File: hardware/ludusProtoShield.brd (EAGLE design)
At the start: 59.7 x 53.3 mm, 65 parts, among them U1 ARDUINO, U2 TB6612FNG

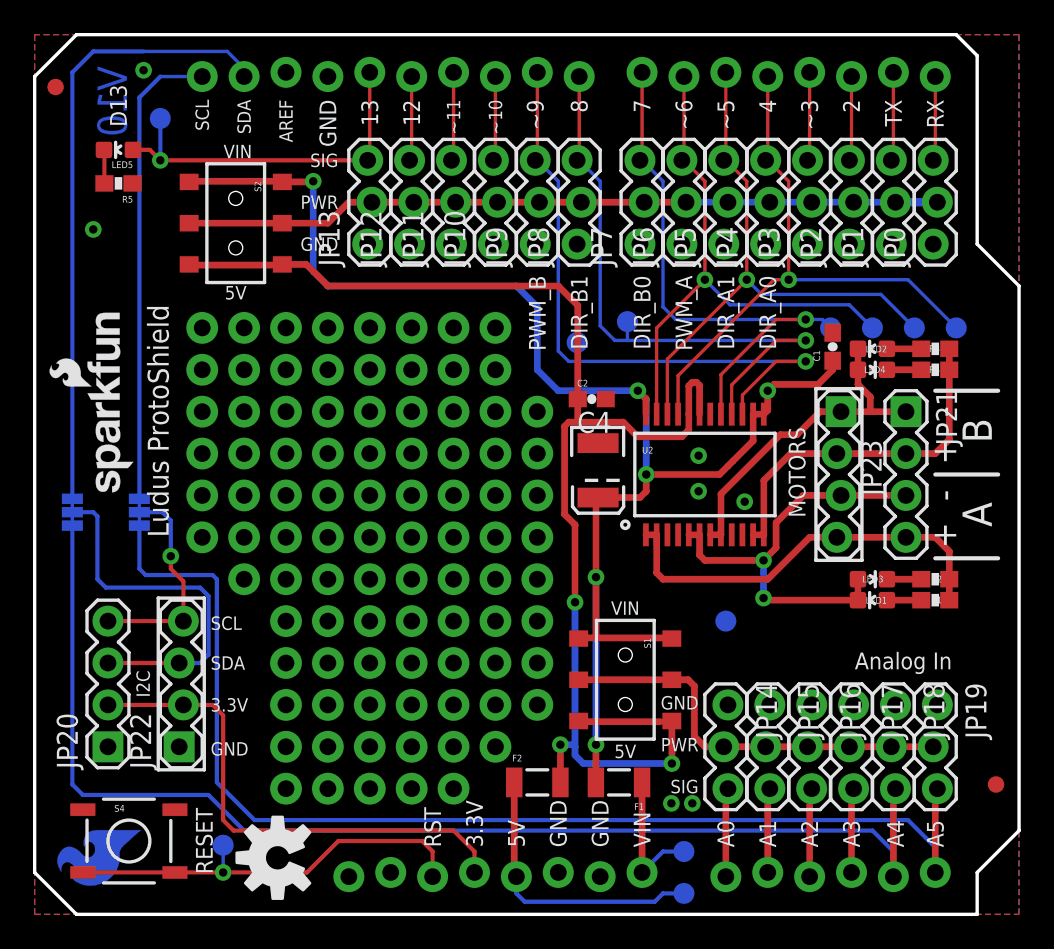
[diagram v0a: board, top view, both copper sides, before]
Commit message: Moved PWM control pins to 3 & 6 instead of 6 & 9
Updated wiring to be compatible with Arduino Servo library. Updated to
ver. 1.1
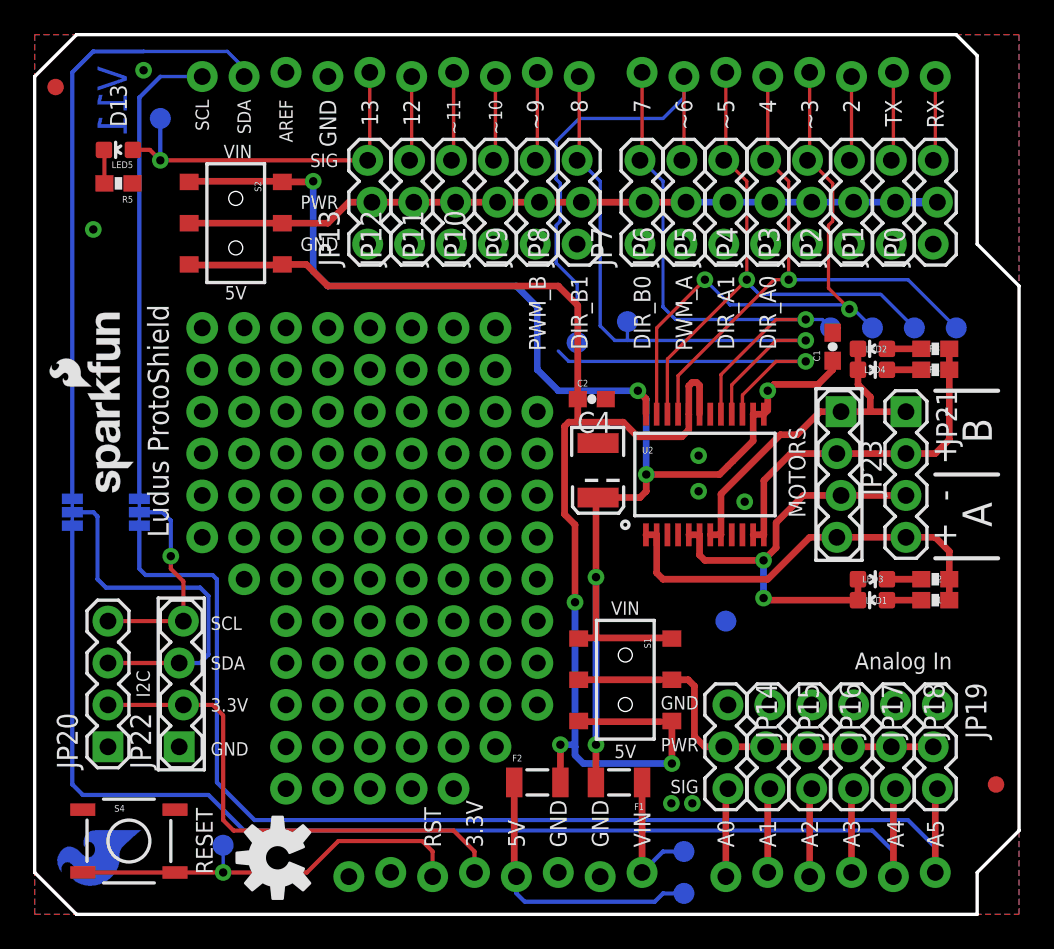
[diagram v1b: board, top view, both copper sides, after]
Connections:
- removed net D3: JP3.3, U1.D3
- new net D9: JP9.3, U1.D9
- net PWMA: now also JP3.3, U1.D3; no longer JP6.3, U1.D6
- net PWMB: now also JP6.3, U1.D6; no longer JP9.3, U1.D9
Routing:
- net PWMB: track 39.9 -> 50.4 mm
- net D3: track 5.39 -> 0.00 mm
- net D9: track 0.00 -> 5.39 mm
- net PWMA: track 33.8 -> 36.5 mm, vias 1 -> 2
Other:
- board text added: "V11"
- board text removed: "V10"
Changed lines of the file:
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@@
 <text x="35.814" y="18.161" size="0.8128" layer="21" font="vector" ratio="15" align="bottom-center">VIN</text>
 <text x="35.814" y="10.287" size="0.8128" layer="21" font="vector" ratio="15" align="top-center">5V</text>
-<text x="5.588" y="51.435" size="1.778" layer="16" font="vector" ratio="15" rot="SMR270">V10</text>
+<text x="5.588" y="51.435" size="1.778" layer="16" font="vector" ratio="15" rot="SMR270">V11</text>
 <text x="37.211" y="-21.717" size="1.778" layer="51" font="vector" ratio="15">B. Huang</text>
 <text x="12.7" y="49.403" size="0.8128" layer="21" ratio="15" rot="R270" align="center-left">SDA</text>
@@
 <signal name="PWMA">
 <contactref element="U2" pad="23"/>
-<contactref element="U1" pad="D6"/>
-<contactref element="JP6" pad="3"/>
-<wire x1="40.64" y1="38.481" x2="40.64" y2="44.45" width="0.2032" layer="1"/>
 <wire x1="37.715" y1="30.326" x2="37.715" y2="35.556" width="0.2032" layer="1"/>
-<wire x1="39.37" y1="50.8" x2="39.37" y2="45.847" width="0.2032" layer="1"/>
-<wire x1="39.37" y1="45.847" x2="39.243" y2="45.72" width="0.2032" layer="1"/>
-<wire x1="39.243" y1="45.72" x2="39.37" y2="45.72" width="0.2032" layer="1"/>
-<wire x1="39.37" y1="45.72" x2="40.64" y2="44.45" width="0.2032" layer="1"/>
 <contactref element="TP3" pad="P$1"/>
 <via x="40.64" y="38.481" extent="1-16" drill="0.508"/>
-<wire x1="50.8" y1="35.56" x2="49.403" y2="36.957" width="0.2032" layer="16"/>
-<wire x1="49.403" y1="36.957" x2="42.164" y2="36.957" width="0.2032" layer="16"/>
 <wire x1="37.715" y1="35.556" x2="40.64" y2="38.481" width="0.2032" layer="1"/>
 <wire x1="42.164" y1="36.957" x2="40.64" y2="38.481" width="0.2032" layer="16"/>
+<contactref element="U1" pad="D3"/>
+<contactref element="JP3" pad="3"/>
+<wire x1="46.99" y1="51.054" x2="46.99" y2="45.847" width="0.2032" layer="1"/>
+<wire x1="46.99" y1="45.847" x2="46.863" y2="45.72" width="0.2032" layer="1"/>
+<via x="49.403" y="36.703" extent="1-16" drill="0.508"/>
+<wire x1="49.403" y1="36.703" x2="48.133" y2="37.973" width="0.2032" layer="1"/>
+<wire x1="48.133" y1="37.973" x2="48.133" y2="41.783" width="0.2032" layer="1"/>
+<wire x1="48.133" y1="41.783" x2="48.387" y2="42.037" width="0.2032" layer="1"/>
+<wire x1="48.387" y1="42.037" x2="48.387" y2="44.323" width="0.2032" layer="1"/>
+<wire x1="46.863" y1="45.72" x2="46.99" y2="45.72" width="0.2032" layer="1"/>
+<wire x1="46.99" y1="45.72" x2="48.387" y2="44.323" width="0.2032" layer="1"/>
+<wire x1="42.164" y1="36.957" x2="49.149" y2="36.957" width="0.2032" layer="16"/>
+<wire x1="49.149" y1="36.957" x2="49.403" y2="36.703" width="0.2032" layer="16"/>
+<wire x1="49.403" y1="36.703" x2="49.657" y2="36.703" width="0.2032" layer="16"/>
+<wire x1="49.657" y1="36.703" x2="50.8" y2="35.56" width="0.2032" layer="16"/>
 </signal>
 <signal name="PWMB">
 <contactref element="U2" pad="15"/>
-<contactref element="U1" pad="D9"/>
-<contactref element="JP9" pad="3"/>
 <via x="46.755" y="33.528" extent="1-16" drill="0.508"/>
-<wire x1="31.75" y1="34.163" x2="31.75" y2="44.45" width="0.2032" layer="16"/>
 <wire x1="42.915" y1="30.326" x2="42.915" y2="31.485" width="0.2032" layer="1"/>
 <wire x1="42.915" y1="31.485" x2="44.958" y2="33.528" width="0.2032" layer="1"/>
@@
 <wire x1="32.385" y1="33.528" x2="32.893" y2="33.528" width="0.2032" layer="16"/>
 <wire x1="32.893" y1="33.528" x2="46.755" y2="33.528" width="0.2032" layer="16"/>
-<wire x1="30.48" y1="51.054" x2="30.48" y2="45.847" width="0.2032" layer="1"/>
-<wire x1="30.48" y1="45.847" x2="30.353" y2="45.72" width="0.2032" layer="1"/>
-<wire x1="30.353" y1="45.72" x2="30.48" y2="45.72" width="0.2032" layer="16"/>
-<wire x1="30.48" y1="45.72" x2="31.75" y2="44.45" width="0.2032" layer="16"/>
 <contactref element="TP6" pad="P$1"/>
 <wire x1="32.893" y1="34.671" x2="32.893" y2="33.528" width="0.2032" layer="16"/>
+<contactref element="U1" pad="D6"/>
+<contactref element="JP6" pad="3"/>
+<wire x1="39.37" y1="50.8" x2="39.37" y2="45.847" width="0.2032" layer="1"/>
+<wire x1="39.37" y1="45.847" x2="39.243" y2="45.72" width="0.2032" layer="1"/>
+<wire x1="32.893" y1="34.671" x2="32.893" y2="38.227" width="0.2032" layer="16"/>
+<wire x1="32.893" y1="38.227" x2="31.623" y2="39.497" width="0.2032" layer="16"/>
+<wire x1="31.623" y1="39.497" x2="31.623" y2="41.783" width="0.2032" layer="16"/>
+<wire x1="31.623" y1="41.783" x2="31.877" y2="42.037" width="0.2032" layer="16"/>
+<wire x1="31.877" y1="42.037" x2="31.877" y2="44.323" width="0.2032" layer="16"/>
+<wire x1="31.877" y1="44.323" x2="31.623" y2="44.577" width="0.2032" layer="16"/>
+<wire x1="31.623" y1="44.577" x2="31.623" y2="46.863" width="0.2032" layer="16"/>
+<wire x1="31.623" y1="46.863" x2="33.02" y2="48.26" width="0.2032" layer="16"/>
+<wire x1="33.02" y1="48.26" x2="38.1" y2="48.26" width="0.2032" layer="16"/>
+<wire x1="38.1" y1="48.26" x2="39.37" y2="49.53" width="0.2032" layer="16"/>
+<wire x1="39.37" y1="49.53" x2="39.37" y2="50.8" width="0.2032" layer="16"/>
 </signal>
 <signal name="VIN">
@@
 <wire x1="38.365" y1="30.326" x2="38.365" y2="33.666" width="0.2032" layer="1"/>
 <wire x1="38.365" y1="33.666" x2="43.18" y2="38.481" width="0.2032" layer="1"/>
+<wire x1="51.308" y1="37.592" x2="43.942" y2="37.592" width="0.2032" layer="16"/>
+<wire x1="53.34" y1="35.56" x2="53.34" y2="35.687" width="0.2032" layer="16"/>
 <wire x1="51.308" y1="37.592" x2="53.34" y2="35.56" width="0.2032" layer="16"/>
-<wire x1="51.308" y1="37.592" x2="44.069" y2="37.592" width="0.2032" layer="16"/>
-<wire x1="44.069" y1="37.592" x2="43.18" y2="38.481" width="0.2032" layer="16"/>
+<wire x1="43.18" y1="38.481" x2="43.18" y2="38.354" width="0.2032" layer="16"/>
+<wire x1="43.18" y1="38.354" x2="43.942" y2="37.592" width="0.2032" layer="16"/>
 </signal>
 <signal name="AIN1">
@@
 <wire x1="11.43" y1="2.54" x2="8.509" y2="2.54" width="0.254" layer="1"/>
 <wire x1="11.43" y1="2.54" x2="11.43" y2="4.191" width="0.2032" layer="16"/>
-</signal>
-<signal name="D3">
-<contactref element="U1" pad="D3"/>
-<contactref element="JP3" pad="3"/>
-<wire x1="46.99" y1="51.054" x2="46.99" y2="45.847" width="0.2032" layer="1"/>
-<wire x1="46.99" y1="45.847" x2="46.863" y2="45.72" width="0.2032" layer="1"/>
 </signal>
 <signal name="A3">
@@
 <wire x1="37.973" y1="11.684" x2="33.02" y2="11.684" width="0.4064" layer="1"/>
 </signal>
+<signal name="D9">
+<contactref element="U1" pad="D9"/>
+<contactref element="JP9" pad="3"/>
+<wire x1="30.48" y1="51.054" x2="30.48" y2="45.847" width="0.2032" layer="1"/>
+<wire x1="30.48" y1="45.847" x2="30.353" y2="45.72" width="0.2032" layer="1"/>
+</signal>
 </signals>

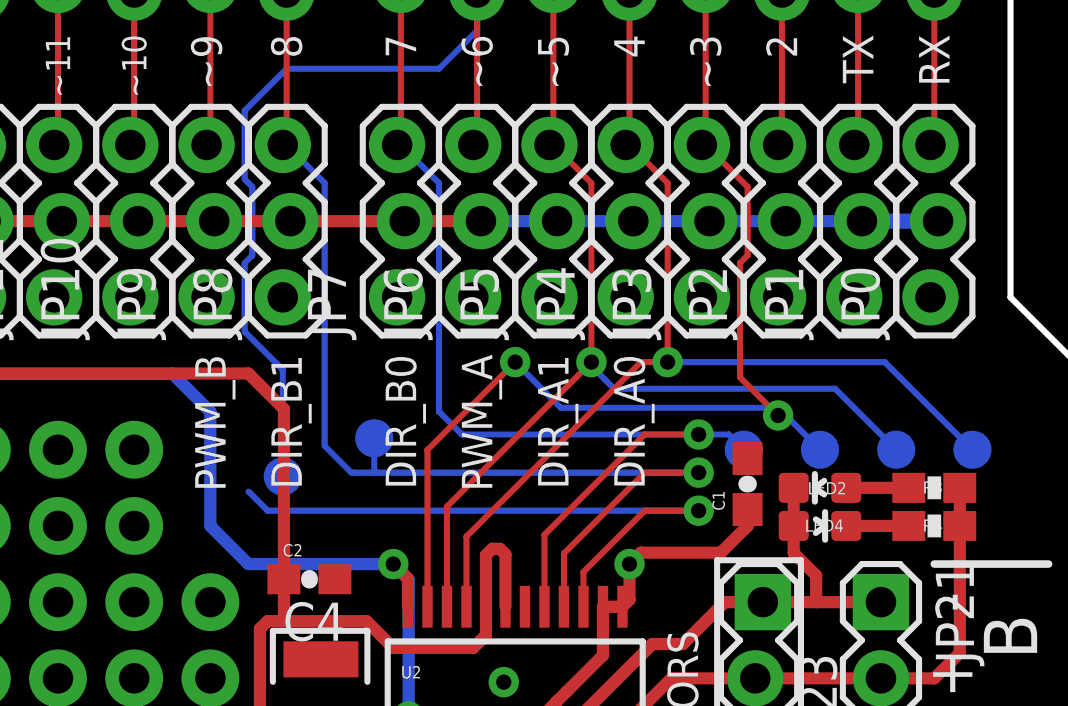
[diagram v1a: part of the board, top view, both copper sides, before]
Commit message: Moved silk to reflect pin change
Updated the silk for PWMA and PWMB
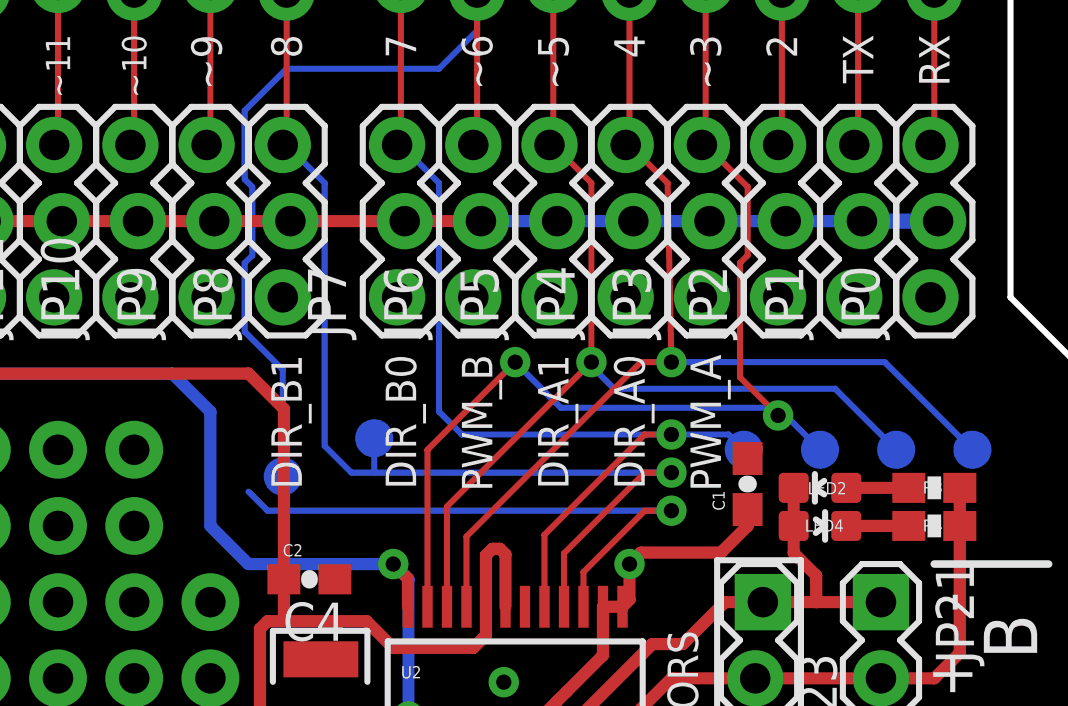
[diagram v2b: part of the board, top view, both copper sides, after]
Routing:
- net PWMB: track 50.4 -> 48.6 mm
- net BIN2: track 37.2 -> 35.4 mm
- net BIN1: track 34.5 -> 33.6 mm
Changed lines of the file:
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@@
 <text x="58.039" y="23.495" size="1.778" layer="21" font="vector" ratio="15" rot="SR90">A</text>
 <text x="41.91" y="38.735" size="1.016" layer="21" font="vector" ratio="15" rot="R90" align="center-right">DIR_A1</text>
-<text x="39.37" y="38.735" size="1.016" layer="21" font="vector" ratio="15" rot="R90" align="center-right">PWM_A</text>
+<text x="46.99" y="38.735" size="1.016" layer="21" font="vector" ratio="15" rot="R90" align="center-right">PWM_A</text>
 <text x="36.83" y="38.735" size="1.016" layer="21" font="vector" ratio="15" rot="R90" align="center-right">DIR_B0</text>
 <text x="33.02" y="38.735" size="1.016" layer="21" font="vector" ratio="15" rot="R90" align="center-right">DIR_B1</text>
-<text x="30.48" y="38.735" size="1.016" layer="21" font="vector" ratio="15" rot="R90" align="center-right">PWM_B</text>
+<text x="39.37" y="38.735" size="1.016" layer="21" font="vector" ratio="15" rot="R90" align="center-right">PWM_B</text>
 <text x="10.795" y="4.445" size="1.016" layer="21" font="vector" ratio="15" rot="R90" align="bottom-center">RESET</text>
 <text x="18.415" y="43.18" size="0.8128" layer="21" font="vector" ratio="15" align="center-right">PWR</text>
@@
 <signal name="PWMB">
 <contactref element="U2" pad="15"/>
-<via x="46.755" y="33.528" extent="1-16" drill="0.508"/>
+<via x="45.847" y="33.528" extent="1-16" drill="0.508"/>
 <wire x1="42.915" y1="30.326" x2="42.915" y2="31.485" width="0.2032" layer="1"/>
 <wire x1="42.915" y1="31.485" x2="44.958" y2="33.528" width="0.2032" layer="1"/>
-<wire x1="46.755" y1="33.528" x2="44.958" y2="33.528" width="0.2032" layer="1"/>
+<wire x1="45.847" y1="33.528" x2="44.958" y2="33.528" width="0.2032" layer="1"/>
 <wire x1="32.385" y1="33.528" x2="31.75" y2="34.163" width="0.2032" layer="16"/>
 <wire x1="32.385" y1="33.528" x2="32.893" y2="33.528" width="0.2032" layer="16"/>
-<wire x1="32.893" y1="33.528" x2="46.755" y2="33.528" width="0.2032" layer="16"/>
+<wire x1="32.893" y1="33.528" x2="45.847" y2="33.528" width="0.2032" layer="16"/>
 <contactref element="TP6" pad="P$1"/>
 <wire x1="32.893" y1="34.671" x2="32.893" y2="33.528" width="0.2032" layer="16"/>
@@
 <contactref element="JP7" pad="3"/>
 <contactref element="U1" pad="D7"/>
-<via x="46.755" y="36.068" extent="1-16" drill="0.508"/>
+<via x="45.847" y="36.068" extent="1-16" drill="0.508"/>
 <wire x1="41.615" y1="30.326" x2="41.615" y2="32.725" width="0.2032" layer="1"/>
 <wire x1="41.615" y1="32.725" x2="44.958" y2="36.068" width="0.2032" layer="1"/>
-<wire x1="46.755" y1="36.068" x2="38.862" y2="36.068" width="0.2032" layer="16"/>
+<wire x1="45.847" y1="36.068" x2="38.862" y2="36.068" width="0.2032" layer="16"/>
 <wire x1="38.862" y1="36.068" x2="38.1" y2="36.83" width="0.2032" layer="16"/>
 <wire x1="38.1" y1="36.83" x2="38.1" y2="44.45" width="0.2032" layer="16"/>
@@
 <wire x1="36.703" y1="45.72" x2="36.83" y2="45.72" width="0.2032" layer="16"/>
 <wire x1="36.83" y1="45.72" x2="38.1" y2="44.45" width="0.2032" layer="16"/>
-<wire x1="46.755" y1="36.068" x2="44.958" y2="36.068" width="0.2032" layer="1"/>
+<wire x1="45.847" y1="36.068" x2="44.958" y2="36.068" width="0.2032" layer="1"/>
 <contactref element="TP4" pad="P$1"/>
-<wire x1="46.755" y1="36.068" x2="47.752" y2="36.068" width="0.2032" layer="16"/>
+<wire x1="45.847" y1="36.068" x2="47.752" y2="36.068" width="0.2032" layer="16"/>
 <wire x1="47.752" y1="36.068" x2="48.26" y2="35.56" width="0.2032" layer="16"/>
 </signal>
@@
 <contactref element="U1" pad="D4"/>
 <contactref element="JP4" pad="3"/>
-<wire x1="45.72" y1="38.481" x2="45.72" y2="44.45" width="0.2032" layer="1"/>
+<wire x1="45.847" y1="38.481" x2="45.72" y2="44.45" width="0.2032" layer="1"/>
 <wire x1="44.45" y1="50.8" x2="44.45" y2="45.847" width="0.2032" layer="1"/>
 <wire x1="44.45" y1="45.847" x2="44.323" y2="45.72" width="0.2032" layer="1"/>
@@
 <wire x1="44.45" y1="45.72" x2="45.72" y2="44.45" width="0.2032" layer="1"/>
 <contactref element="TP1" pad="P$1"/>
-<via x="45.72" y="38.481" extent="1-16" drill="0.508"/>
+<via x="45.847" y="38.481" extent="1-16" drill="0.508"/>
 <wire x1="39.015" y1="30.326" x2="39.015" y2="32.665" width="0.2032" layer="1"/>
 <wire x1="39.015" y1="32.665" x2="44.831" y2="38.481" width="0.2032" layer="1"/>
-<wire x1="44.831" y1="38.481" x2="45.72" y2="38.481" width="0.2032" layer="1"/>
-<wire x1="45.72" y1="38.481" x2="52.959" y2="38.481" width="0.2032" layer="16"/>
+<wire x1="44.831" y1="38.481" x2="45.847" y2="38.481" width="0.2032" layer="1"/>
+<wire x1="45.847" y1="38.481" x2="52.959" y2="38.481" width="0.2032" layer="16"/>
 <wire x1="52.959" y1="38.481" x2="55.88" y2="35.56" width="0.2032" layer="16"/>
 </signal>
@@
 <contactref element="JP8" pad="3"/>
 <contactref element="U1" pad="D8"/>
-<via x="46.755" y="34.798" extent="1-16" drill="0.508"/>
+<via x="45.847" y="34.798" extent="1-16" drill="0.508"/>
 <wire x1="34.29" y1="35.687" x2="34.29" y2="44.45" width="0.2032" layer="16"/>
 <wire x1="42.265" y1="30.326" x2="42.265" y2="32.105" width="0.2032" layer="1"/>
 <wire x1="42.265" y1="32.105" x2="44.958" y2="34.798" width="0.2032" layer="1"/>
-<wire x1="46.755" y1="34.798" x2="44.958" y2="34.798" width="0.2032" layer="1"/>
+<wire x1="45.847" y1="34.798" x2="44.958" y2="34.798" width="0.2032" layer="1"/>
 <wire x1="35.179" y1="34.798" x2="34.29" y2="35.687" width="0.2032" layer="16"/>
 <wire x1="35.179" y1="34.798" x2="35.941" y2="34.798" width="0.2032" layer="16"/>
-<wire x1="36.068" y1="34.798" x2="46.755" y2="34.798" width="0.2032" layer="16"/>
+<wire x1="35.941" y1="34.798" x2="45.847" y2="34.798" width="0.2032" layer="16"/>
 <wire x1="33.02" y1="50.8" x2="33.02" y2="45.847" width="0.2032" layer="1"/>
 <wire x1="33.02" y1="45.847" x2="32.893" y2="45.72" width="0.2032" layer="1"/>
@@
 <contactref element="TP5" pad="P$1"/>
 <wire x1="35.941" y1="35.941" x2="35.941" y2="34.798" width="0.2032" layer="16"/>
-<wire x1="35.941" y1="34.798" x2="36.068" y2="34.798" width="0.2032" layer="16"/>
 </signal>
 <signal name="N$20">
